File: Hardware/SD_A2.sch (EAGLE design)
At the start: 32 parts, among them IC1 74LS245N, IC2 LM317, IC3 2716 / 2732, IC4 XC9572XL

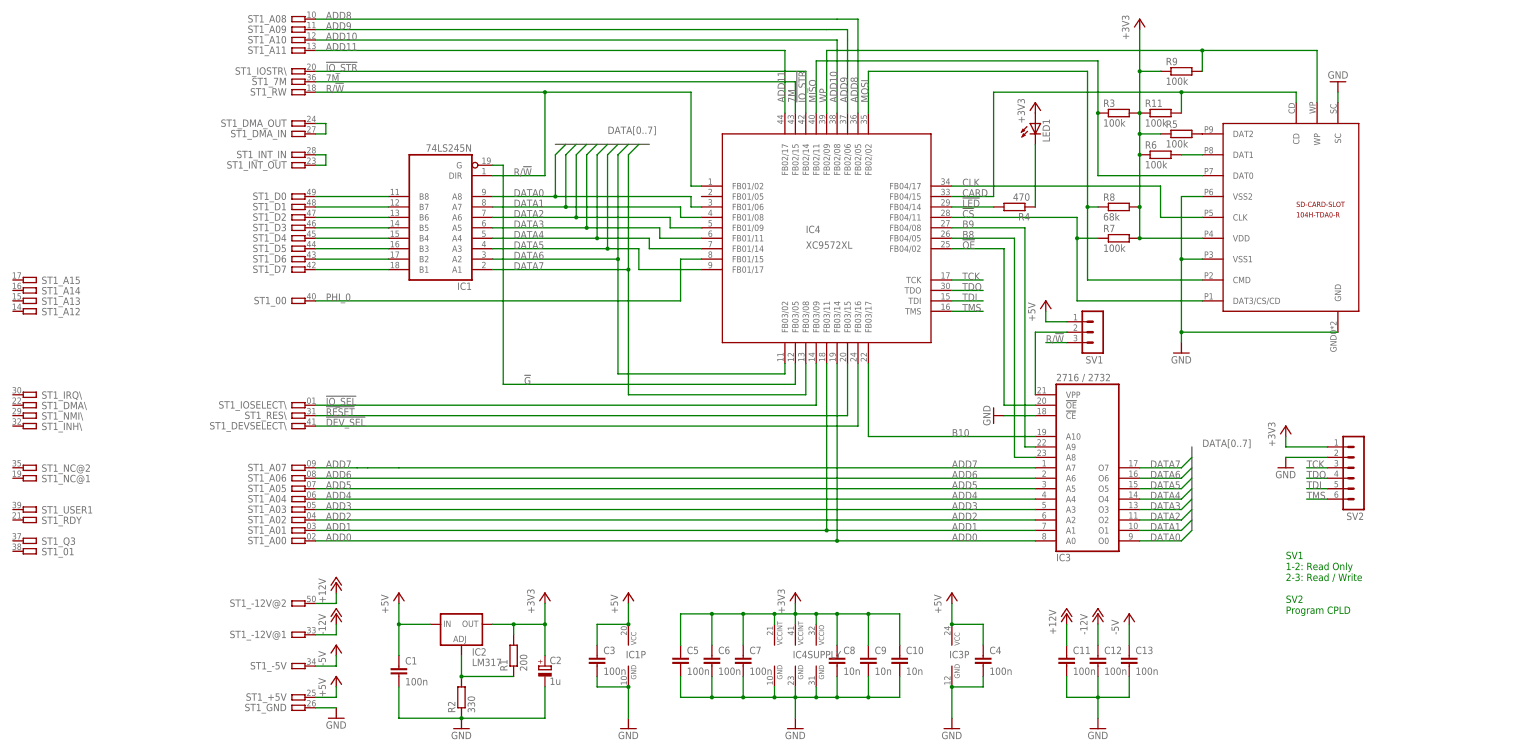
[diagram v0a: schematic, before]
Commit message: Replace CPLD with MC6852 and add Level Shifting microSD Breakout.
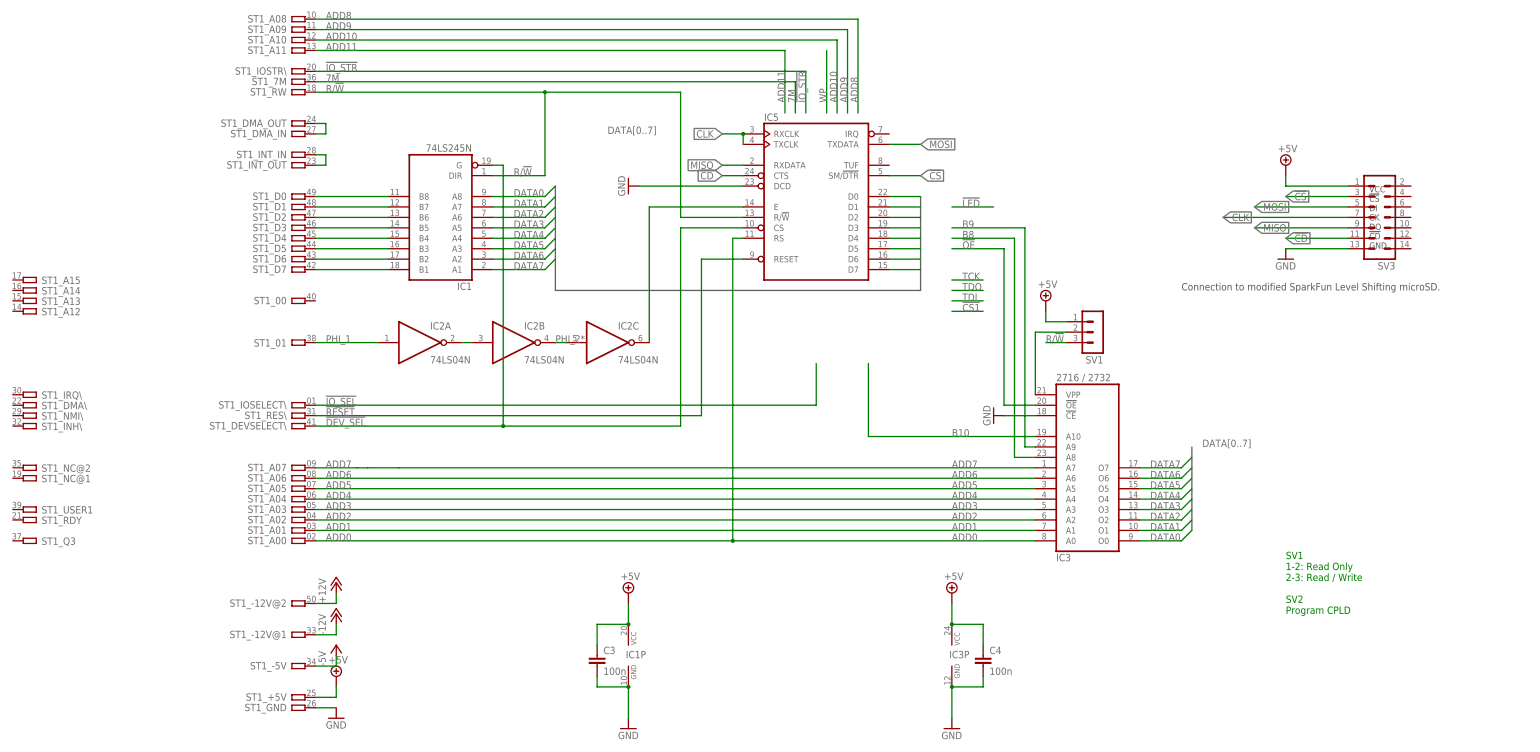
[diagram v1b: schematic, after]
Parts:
- removed C1, C11, C12, C13, C5, C6, C7: 100n, rcl:C-EUC0603K
- removed C10, C8, C9: 10n, rcl:C-EUC0603K
- removed C2: 1u, rcl:CPOL-EU153CLV-0405
- removed IC4: XC9572XL, xilinx-xc9:XC9572_S44
- removed LED1: (no value), led:LEDSQR2X5
- removed R1: 200, rcl:R-EU_R0603
- removed R11, R3, R5, R6, R7, R9: 100k, rcl:R-EU_R0603
- removed R2: 330, rcl:R-EU_R0603
- removed R4: 470, rcl:R-EU_R0603
- removed R8: 68k, rcl:R-EU_R0603
- removed SV2: (no value), con-lstb:MA06-1
- removed U$2: 104H-TDA0-R, con-sd-attend2:104H-TDA0-R
- added IC5: (no value), micro-motorola:6852
- added SV3: (no value), con-lstb:MA07-2
- IC2: value LM317 -> 74LS04N; device v-reg:LM317TL -> 74xx-us:74LS04N
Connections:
- removed net !G: IC1A.G, IC4G$1.FB03/05
- removed net !LED: IC4G$1.FB04/14, R4.2
- removed net +3V3: C10.1, C2.+, C5.1, C6.1, C7.1, C8.1, C9.1, IC2.OUT, IC4SUPPLY.VCCINT@0, IC4SUPPLY.VCCINT@1, IC4SUPPLY.VCCIO, LED1.A, R1.2, R11.1, R3.2, R5.1, R6.1, R7.2, R8.2, R9.1, SV2.1, U$2.VDD
- removed net CARD: IC4G$1.FB04/15, R11.2, U$2.CD
- removed net N$29: LED1.C, R4.1
- removed net N$3: R6.2, U$2.DAT1
- removed net PHI_0: IC4G$1.FB01/15, ST1_00.P
- removed net TCK: IC4G$1.TCK, SV2.3
- removed net TDI: IC4G$1.TDI, SV2.5
- removed net TDO: IC4G$1.TDO, SV2.4
- removed net TMS: IC4G$1.TMS, SV2.6
- removed net WP: IC4G$1.FB02/09, R9.2, U$2.WP
- new net !CD: IC5A.CTS, SV3.11
- new net PHI_1: IC2A.I, ST1_01.P
- new net PHI_2*: IC2C.O, IC5A.E
- net !CS: now also IC5A.SM/!DTR, SV3.3; no longer IC4G$1.FB04/11, R7.1, U$2.DAT3/CS/CD
- net !DEV_SEL: now also IC1A.G, IC5A.CS; no longer IC4G$1.FB03/16
- net !IO_SEL: no longer IC4G$1.FB03/09
- net !IO_STR: no longer IC4G$1.FB02/14
- net !OE: no longer IC4G$1.FB04/02
- net !RESET: now also IC5A.RESET; no longer IC4G$1.FB03/15
- net +12V: no longer C11.1
- net +5V: now also SV3.1; no longer C1.1, IC2.IN
- net -12V: no longer C12.1
- net -5V: no longer C13.1
- net 7M: no longer IC4G$1.FB02/15
- net ADD0: now also IC5A.RS; no longer IC4G$1.FB03/14
- net ADD1: no longer IC4G$1.FB03/11
- net ADD10: no longer IC4G$1.FB02/08
- net ADD11: no longer IC4G$1.FB02/17
- net ADD8: no longer IC4G$1.FB02/05
- net ADD9: no longer IC4G$1.FB02/06
- net B10: no longer IC4G$1.FB03/17
- net B8: no longer IC4G$1.FB04/05
- net B9: no longer IC4G$1.FB04/08
- net CLK: now also IC5A.RXCLK, IC5A.TXCLK, SV3.7; no longer IC4G$1.FB04/17, U$2.CLK
- net DATA0: now also IC5A.D0; no longer IC4G$1.FB01/06
- net DATA1: now also IC5A.D1; no longer IC4G$1.FB01/08
- net DATA2: now also IC5A.D2; no longer IC4G$1.FB01/09
- net DATA3: now also IC5A.D3; no longer IC4G$1.FB01/11
- net DATA4: now also IC5A.D4; no longer IC4G$1.FB01/14
- net DATA5: now also IC5A.D5; no longer IC4G$1.FB01/17
- net DATA6: now also IC5A.D6; no longer IC4G$1.FB03/02
- net DATA7: now also IC5A.D7; no longer IC4G$1.FB03/08
- net GND: now also IC5A.DCD, SV3.13; no longer C1.2, C10.2, C11.2, C12.2, C13.2, C2.-, C5.2, C6.2, C7.2, C8.2, C9.2, IC4SUPPLY.GND@0, IC4SUPPLY.GND@1, IC4SUPPLY.GND@2, R2.1, SV2.2, U$2.GND, U$2.SC, U$2.VSS1, U$2.VSS2
- net MISO: now also IC5A.RXDATA, SV3.9; no longer IC4G$1.FB02/11, R3.1, U$2.DAT0
- net MOSI: now also IC5A.TXDATA, SV3.5; no longer IC4G$1.FB02/02, R8.1, U$2.CMD
- net N$1: now also IC2A.O, IC2B.I; no longer IC2.ADJ, R1.1, R2.2
- net N$2: now also IC2B.O, IC2C.I; no longer R5.2, U$2.DAT2
- net R/!W: now also IC5A.R/!W; no longer IC4G$1.FB01/02
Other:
- note added: "Connection to modified SparkFun Level Shifting microSD."
- note added: "VCC !CS DI CK DO !CD GND"
- moved on the sheet: ST1_01
